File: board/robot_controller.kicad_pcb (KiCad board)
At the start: 2 copper layers, 314 parts, among them J101 CONN_2, J102 CONN_2, J103 CONN_2, J104 JTAG-ARM, J105 CONN_2, J106 USBCONN, J107 CONN_8, J108 CONN_8, J109 USBCONN, J110 CONN_4, J111 UEXT, J112 UEXT, J113 CONN_4, J201 CONN_2, J2301 CONN_STEPPER, J2302 CONN_2, J2401 CONN_STEPPER, J2402 CONN_2, J2501 CONN_STEPPER, J2502 CONN_2, J2601 CONN_STEPPER, J2602 CONN_2, J301 CONN_2, P102 CONN_1, P103 CONN_1, P104 CONN_1, P105 CONN_1, P106 CONN_1, P107 CONN_1, P108 CONN_1, P109 CONN_1, P110 CONN_1, P111 CONN_1, P112 CONN_1, P113 CONN_1, P114 CONN_1, P115 CONN_1, P116 CONN_1, P117 CONN_1, P118 CONN_1, P119 CONN_1, P120 CONN_1, P121 CONN_1, P122 CONN_1, P123 CONN_1, P124 CONN_1, P125 CONN_1, P126 CONN_1, P127 CONN_1, P128 CONN_1, P129 CONN_1, P130 CONN_1, Q101 PNP, Q1501 NJT4031NT1G, Q1601 NJT4031NT1G, Q1701 NJT4031NT1G, Q1801 NJT4031NT1G, Q1901 NJT4031NT1G, Q2001 NJT4031NT1G, Q2101 NJT4031NT1G, Q2201 NJT4031NT1G, Q401 MMBT5962, Q402 MMBT5962, Q501 MMBT5962, Q502 MMBT5962, SW101 SPST, SW102 SPST, SW103 SPST, SW104 SPST, SW105 SPST, SW106 SPST, U101 STM32F405-144, U102 FT232RL, U201 MAX6675, U2301 L6470, U2401 L6470, U2501 L6470, U2601 L6470, U301 MAX6675, U601 LMZ14201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

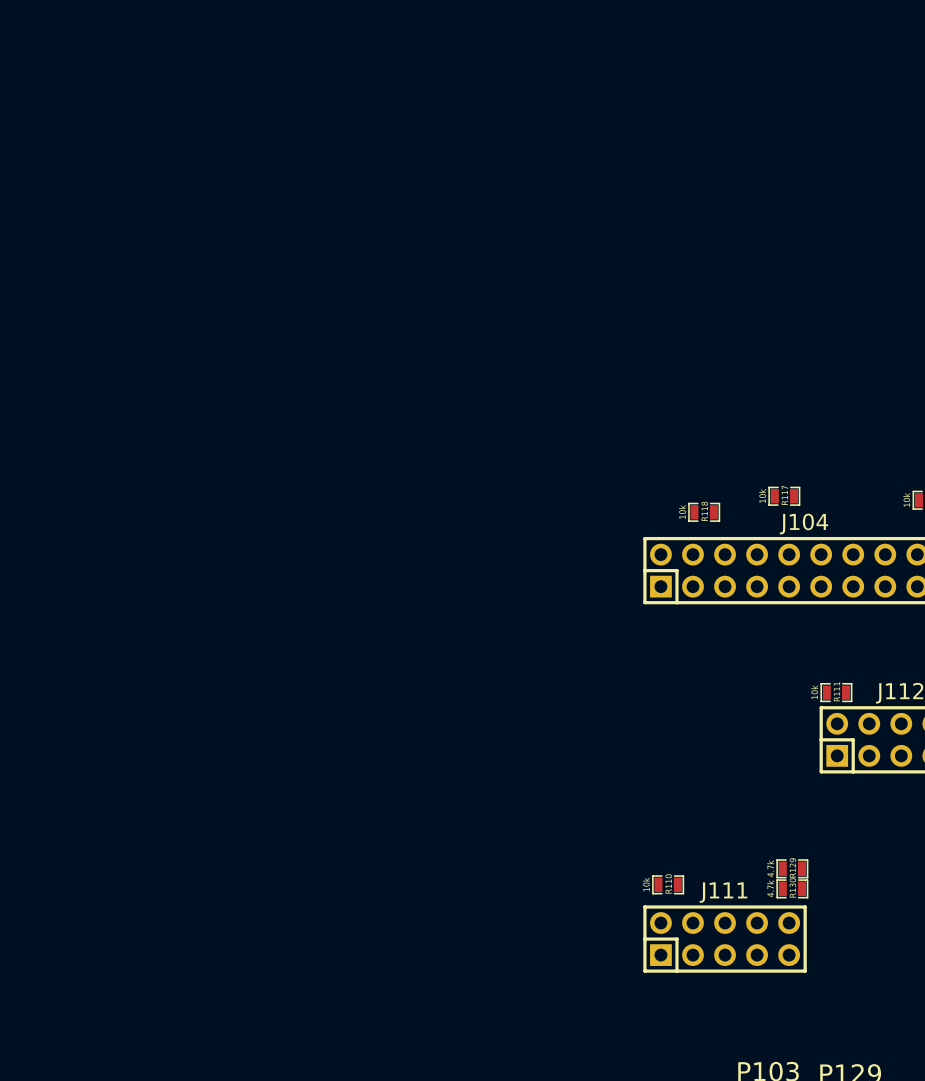
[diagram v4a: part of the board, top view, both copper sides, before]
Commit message: SOLDER_BRIDGE Footprint
Added the SOLDER_BRIDGE footprint to our component library. I added it
to the layout as well.
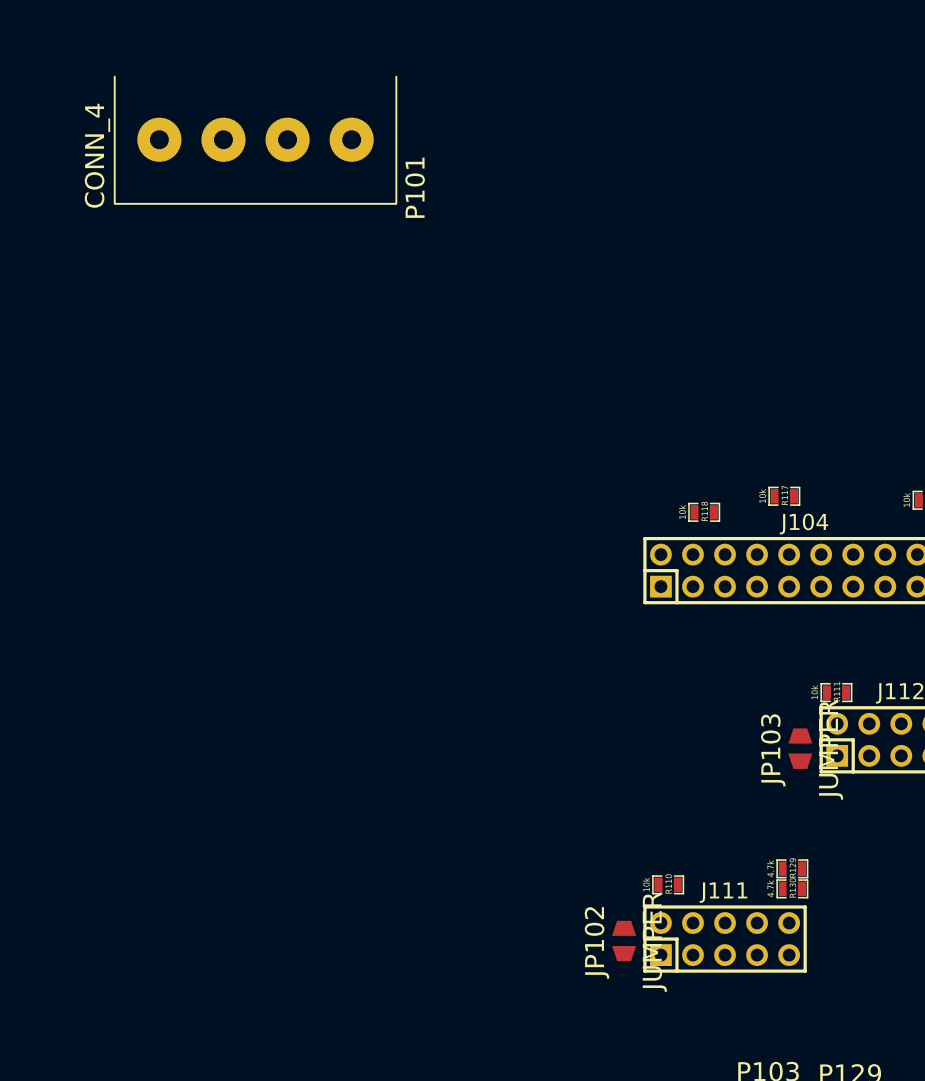
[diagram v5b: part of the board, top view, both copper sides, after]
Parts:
- added JP102: JUMPER, components:SOLDER_BRIDGE, F.Cu at (15.2, 53.7)
- added JP103: JUMPER, components:SOLDER_BRIDGE, F.Cu at (29.2, 38.4)
- added P101: CONN_4, components:SCONN_4, F.Cu at (-14.0, -9.84)
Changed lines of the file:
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@@
 (kicad_pcb (version 3) (host pcbnew "(2014-01-30 BZR 4648)-product")
   (general
-    (links 781)
-    (no_connects 606)
+    (links 789)
+    (no_connects 613)
     (area 0 0 0 0)
     (thickness 1.6)
@@
     (tracks 1030)
     (zones 0)
-    (modules 314)
+    (modules 317)
     (nets 238)
   )
@@
       (net 2 +3.3V))
   )
+  (module components:SOLDER_BRIDGE (layer F.Cu)
+    (at 15.24 53.6575 90)
+    (fp_text reference JP102 (at 0 -2.286 90) (layer F.SilkS)
+      (effects (font (size 1.5 1.5) (thickness 0.15)))
+    )
+    (fp_text value JUMPER (at 0 2.286 90) (layer F.SilkS)
+      (effects (font (size 1.5 1.5) (thickness 0.15)))
+    )
+    (pad 1 smd trapezoid (at -1 0 90) (size 1.2 1.5) (rect_delta -0.4 0 ) (layers F.Cu F.Paste F.Mask)
+      (net 161 "Net-(J111-Pad1)"))
+    (pad 2 smd trapezoid (at 1 0 90) (size 1.2 1.5) (rect_delta 0.4 0 ) (layers F.Cu F.Paste F.Mask)
+      (net 2 +3.3V))
+  )
+  (module components:SOLDER_BRIDGE (layer F.Cu)
+    (at 29.21 38.4175 90)
+    (fp_text reference JP103 (at 0 -2.286 90) (layer F.SilkS)
+      (effects (font (size 1.5 1.5) (thickness 0.15)))
+    )
+    (fp_text value JUMPER (at 0 2.286 90) (layer F.SilkS)
+      (effects (font (size 1.5 1.5) (thickness 0.15)))
+    )
+    (pad 1 smd trapezoid (at -1 0 90) (size 1.2 1.5) (rect_delta -0.4 0 ) (layers F.Cu F.Paste F.Mask)
+      (net 162 "Net-(J112-Pad1)"))
+    (pad 2 smd trapezoid (at 1 0 90) (size 1.2 1.5) (rect_delta 0.4 0 ) (layers F.Cu F.Paste F.Mask)
+      (net 2 +3.3V))
+  )
+  (module components:SCONN_4 (layer F.Cu)
+    (at -13.97 -9.8425)
+    (fp_text reference P101 (at 12.7 3.81 90) (layer F.SilkS)
+      (effects (font (size 1.5 1.5) (thickness 0.15)))
+    )
+    (fp_text value CONN_4 (at -12.7 1.27 90) (layer F.SilkS)
+      (effects (font (size 1.5 1.5) (thickness 0.15)))
+    )
+    (fp_line (start -11.16 5.08) (end 11.16 5.08) (layer F.SilkS) (width 0.15))
+    (fp_line (start 11.16 5) (end 11.16 -5) (layer F.SilkS) (width 0.15))
+    (fp_line (start -11.16 5) (end -11.16 -5) (layer F.SilkS) (width 0.15))
+    (pad 2 thru_hole circle (at 2.54 0) (size 3.5 3.5) (drill 1.5) (layers *.Cu *.Mask F.SilkS)
+      (net 50 "/LED Data 1/DATA_OUT"))
+    (pad 1 thru_hole circle (at 7.62 0) (size 3.5 3.5) (drill 1.5) (layers *.Cu *.Mask F.SilkS)
+      (net 48 "/LED Data 0/DATA_OUT"))
+    (pad 3 thru_hole circle (at -2.54 0) (size 3.5 3.5) (drill 1.5) (layers *.Cu *.Mask F.SilkS)
+      (net 119 GND))
+    (pad 4 thru_hole circle (at -7.62 0) (size 3.5 3.5) (drill 1.5) (layers *.Cu *.Mask F.SilkS)
+      (net 119 GND))
+  )
   (segment (start 62.23 -40.3225) (end 99.06 -40.3225) (width 0.4064) (layer B.Cu) (net 0))

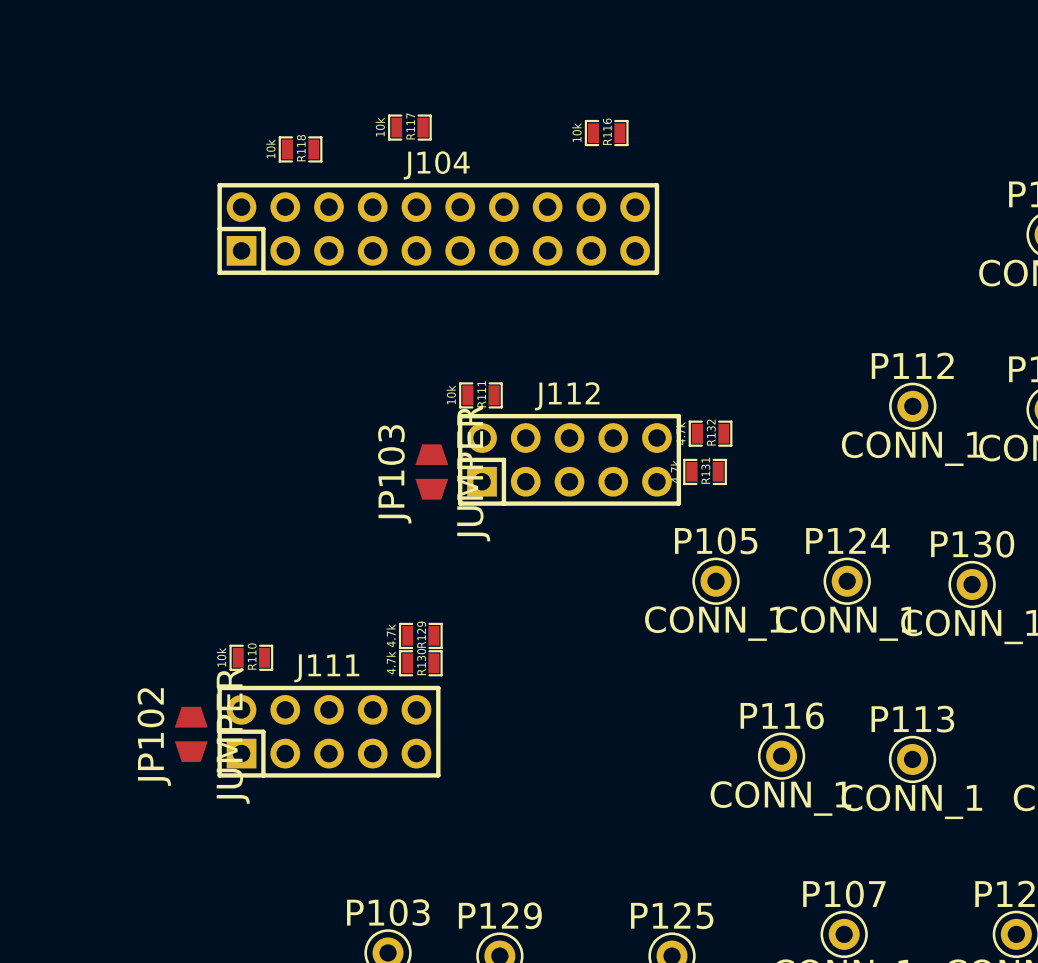
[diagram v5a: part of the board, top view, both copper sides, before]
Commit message: SHROUDED_10 and SHROUDED_20 Footprints
Created two footprints for the UEXT and JTAG connectors.
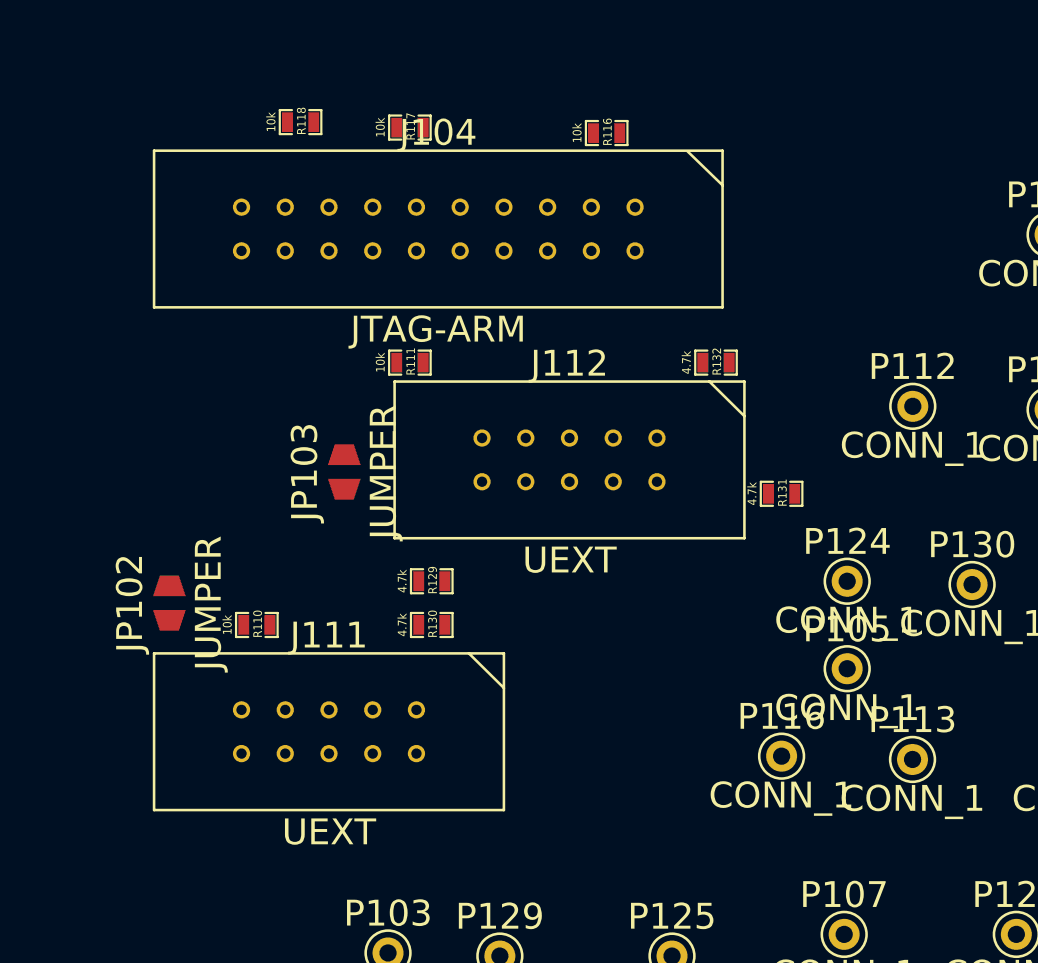
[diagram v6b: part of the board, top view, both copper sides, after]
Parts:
- J104: footprint Pin_Headers:Pin_Header_Straight_2x10 -> components:SHROUDED_20
- J111, J112: footprint Pin_Headers:Pin_Header_Straight_2x05 -> components:SHROUDED_10
- moved P105 9.16 mm to (53.3, 49.8)
- moved JP102 7.73 mm to (14.0, 46.0)
- moved JP103 5.08 mm to (24.1, 38.4)
- moved R131 4.62 mm to (49.5, 39.7)
- moved R111 4.55 mm to (27.9, 32.1)
- moved R132 4.14 mm to (45.7, 32.1)
- moved R129 3.24 mm to (29.2, 44.8)
- moved R130 2.31 mm to (29.2, 47.3)
- moved R110 1.93 mm to (19.1, 47.3)
- moved R118 1.59 mm to (21.6, 18.1)

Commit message: Named all connectors/leds/switches based on their functionality, refdes's are safe.
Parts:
- removed P101: CONN_4, components:SCONN_4
- removed P127, P128, P129: CONN_1, components:MINI_TP
- added TP115: GND, components:MINI_TP, F.Cu at (4.76, 6.67)
- added TP116: GND, components:MINI_TP, F.Cu at (2.86, 2.86)
- added TP117: GND, components:MINI_TP, F.Cu at (8.57, 4.13)
- D101: value LED_BLUE -> LED0
- D102: value LED_BLUE -> LED1
- D103: value LED_BLUE -> LED2
- D104: value LED_BLUE -> LED3
- D105: value LED_WHITE -> Power
- D106: value LED_GREEN -> TX
- D107: value LED_RED -> RX
- D2302, D2402, D2502, D2602: value LED_RED -> Error
- D2303, D2403, D2503, D2603: value LED_GREEN -> Busy
- J101: value CONN_2 -> +3.3V
- J102: value CONN_2 -> +24V
- J103: value CONN_2 -> GND
- J105: value CONN_2 -> Power
- J106: value USBCONN -> FTDI-USB
- J107: value CONN_8 -> Industrial Inputs
- J108: value CONN_8 -> Industrial Outputs
- J109: value USBCONN -> MCU-USB
- J110: value CONN_4 -> AUX-UART
- J111: value UEXT -> UEXT0
- J112: value UEXT -> UEXT1
- J113: value CONN_4 -> RGB LEDs
- J201, J301: value CONN_2 -> Temp Probe
- J2301, J2401, J2501, J2601: value CONN_STEPPER -> Stepper Motor
- J2302, J2402, J2502, J2602: value CONN_2 -> Limit-SW
- SW101: value SPST -> SW0
- SW102: value SPST -> SW1
- SW103: value SPST -> SW2
- SW104: value SPST -> SW3
- SW105: value SPST -> RESET
- SW106: value SPST -> BOOT
- TP101: renamed from P102; value CONN_1 -> STEPPERS_SCK
- TP102: renamed from P106; value CONN_1 -> STEPPERS_MOSI
- TP103: renamed from P110; value CONN_1 -> STEPPERS_MISO
- TP104: renamed from P114; value CONN_1 -> STEPPER0-~CS
- TP105: renamed from P118; value CONN_1 -> STEPPER1-~CS
- TP106: renamed from P122; value CONN_1 -> STEPPER2-~CS
- TP107: renamed from P126; value CONN_1 -> STEPPER3-~CS
- TP108: renamed from P103; value CONN_1 -> STEPPER0_STCK
- TP109: renamed from P107; value CONN_1 -> STEPPER1_STCK
- TP110: renamed from P111; value CONN_1 -> STEPPER2_STCK
- TP111: renamed from P115; value CONN_1 -> STEPPER3_STCK
- TP112: renamed from P119; value CONN_1 -> STEPPERS_OSCIN
- TP113: renamed from P123; value CONN_1 -> STEPPERS_OSC_SYNC
- TP114: renamed from P130; value CONN_1 -> GND
- TP118: renamed from P105; value CONN_1 -> USART1_RX
- TP119: renamed from P109; value CONN_1 -> USART1_TX
- TP120: renamed from P113; value CONN_1 -> USART1_CTS
- TP121: renamed from P117; value CONN_1 -> USART1_RTS
- TP122: renamed from P121; value CONN_1 -> LED_DATA0
- TP123: renamed from P125; value CONN_1 -> LED_DATA1
- TP124: renamed from P104; value CONN_1 -> TEMP_MISO
- TP125: renamed from P108; value CONN_1 -> TEMP_SCK
- TP126: renamed from P112; value CONN_1 -> TEMP0-~CS
- TP127: renamed from P116; value CONN_1 -> TEMP1-~CS
- TP128: renamed from P120; value CONN_1 -> SUPPLY_SENSE
- TP129: renamed from P124; value CONN_1 -> STEPPERS_SENSE
- moved TP129 177.1 mm to (183.5, -75.2)
- moved TP120 173.2 mm to (71.4, -117.5)
- moved TP119 164.9 mm to (62.2, -119.7)
- moved TP118 164.5 mm to (54.0, -114.6)
- moved TP128 157.8 mm to (183.2, -69.8)
- moved TP121 146.9 mm to (65.1, -111.8)
- moved TP127 131.8 mm to (52.1, -76.8)
- moved TP126 128.4 mm to (52.4, -93.7)
- moved TP124 119.2 mm to (52.4, -86.7)
- moved TP123 113.7 mm to (48.9, -47.0)
- moved TP104 108.1 mm to (17.8, 98.4)
- moved TP125 105.7 mm to (52.7, -80.3)
- moved TP122 84.7 mm to (55.2, -54.6)
- moved TP107 78.9 mm to (75.6, 97.8)
- moved TP113 78.0 mm to (58.1, 103.5)
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- renumbered JP102 to JP101, JP103 to JP102

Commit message: More work on the stepper motors. Organized a lot of labels. Preparing for copying stepper motors.
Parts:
- J201: value Temp Probe -> Temp 0
- J2301: value Stepper Motor -> Motor 0
- J2302: value Limit-SW -> Limit SW 0
- TP118: value USART1_RX -> RX
- TP119: value USART1_TX -> TX
- TP120: value USART1_CTS -> CTS
- TP121: value USART1_RTS -> RTS
- dJ301: renamed from J301; value Temp Probe -> Temp 1
- moved TP114 197.1 mm to (62.9, -116.5)
- moved TP117 94.9 mm to (53.7, -79.4)
- moved R107 74.7 mm to (86.0, 53.3), turned to 270 degrees
- moved D104 69.6 mm to (87.9, 53.3), turned to 90 degrees
- moved R104 67.5 mm to (94.6, 53.3), turned to 270 degrees
- moved SW102 66.0 mm to (105.1, 46.7), turned to 270 degrees
- moved D103 62.6 mm to (96.5, 53.3), turned to 90 degrees
- moved C104 61.2 mm to (89.9, 53.3), turned to 90 degrees
- moved R102 60.7 mm to (103.2, 53.3), turned to 270 degrees
- moved SW103 57.5 mm to (96.5, 46.7), turned to 270 degrees
- moved SW106 57.2 mm to (96.5, 35.2), turned to 270 degrees
- moved D102 56.1 mm to (105.1, 53.3), turned to 90 degrees
- moved SW101 55.3 mm to (113.7, 46.7), turned to 270 degrees
- moved C103 54.6 mm to (98.4, 53.3), turned to 90 degrees
- moved R101 54.6 mm to (111.8, 53.3), turned to 270 degrees
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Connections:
- J2302 pad 1: GND -> Net-(J2302-Pad1)
- J2302 pad 2: Net-(J2302-Pad2) -> GND
- J2402 pad 1: GND -> Net-(J2402-Pad1)
- J2402 pad 2: Net-(J2402-Pad2) -> GND
- J2502 pad 1: GND -> Net-(J2502-Pad1)
- J2502 pad 2: Net-(J2502-Pad2) -> GND
- J2602 pad 1: GND -> Net-(J2602-Pad1)
- J2602 pad 2: Net-(J2602-Pad2) -> GND
- R2307 pad 1: Net-(J2302-Pad2) -> Net-(J2302-Pad1)
- R2407 pad 1: Net-(J2402-Pad2) -> Net-(J2402-Pad1)
- R2507 pad 1: Net-(J2502-Pad2) -> Net-(J2502-Pad1)
- R2607 pad 1: Net-(J2602-Pad2) -> Net-(J2602-Pad1)
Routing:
- net GND: track 261.8 -> 287.4 mm
- net Net-(J106-Pad3): track 0.00 -> 12.3 mm
- net /LED Data 1/DATA_OUT: track 10.3 -> 22.5 mm
- net Net-(J301-Pad2): track 0.00 -> 10.7 mm
- net Net-(J106-Pad2): track 0.00 -> 9.72 mm
- net Net-(J201-Pad2): track 0.00 -> 9.21 mm
- net Net-(J2302-Pad2): track 8.25 -> 0.00 mm
- net Net-(J2302-Pad1): track 0.00 -> 6.49 mm
- net /USART1_CTS: track 4.03 -> 9.86 mm
- net /SW0: track 0.00 -> 5.74 mm
- net /SW3: track 0.00 -> 5.74 mm
- net /SW2: track 0.00 -> 5.74 mm
- net /SW1: track 0.00 -> 5.74 mm
- net /USART1_RTS: track 3.47 -> 9.09 mm
- net /LED Data 0/DATA_OUT: track 16.4 -> 21.9 mm
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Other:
- board text added: "0"
- board text added: "Motor 0"
- board text added: "USART1"
